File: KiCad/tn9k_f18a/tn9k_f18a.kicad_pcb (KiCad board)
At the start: 2 copper layers, 27.9 x 88.3 mm, 9 parts, among them J1 Conn_01x20, J2 Conn_01x20, J3 Conn_01x24, J4 Conn_01x24, J5 Conn_02x04_Counter_Clockwise, J6 Conn_02x08_Odd_Even, U1 SN74LVC245, U2 SN74LVC245, U3 SN74LVC245

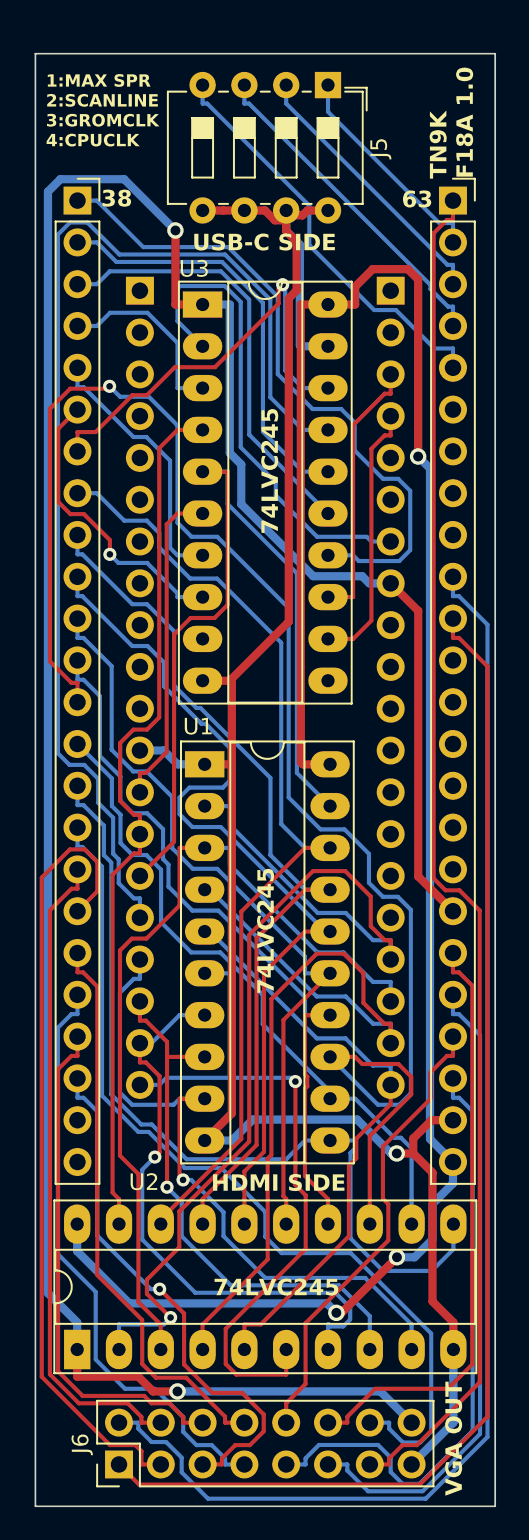
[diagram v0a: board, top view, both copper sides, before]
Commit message: update original board adding diode
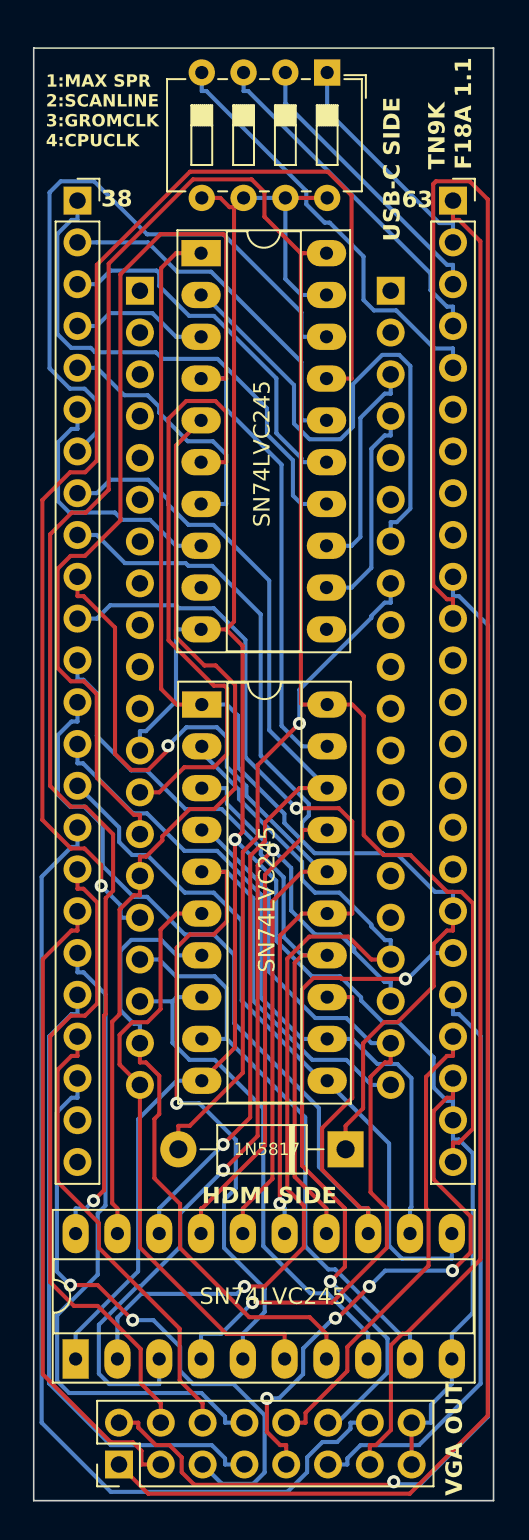
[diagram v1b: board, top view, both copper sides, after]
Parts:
- added D1: 1N5817, Diode_THT:D_DO-41_SOD81_P10.16mm_Horizontal, F.Cu at (166.2, 107.8)
- moved U2 39.9 mm to (157.4, 80.8), turned to 0 degrees
- moved U1 37.0 mm to (149.8, 120.6), turned to 90 degrees
- moved U3 3.12 mm to (157.4, 53.4)
- moved J5 0.76 mm to (165.0, 42.4)
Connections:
- J4 pad 18: VCC -> VDD
- J6 pad 16: VCC -> GND
- U2 pad 1: VCC -> VDD
- U3 pad 1: VCC -> VDD
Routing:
- net VCC: track 156.4 -> 40.4 mm, vias 2 -> 1
- net VDD: track 0.00 -> 72.4 mm
- net R0_3V3: track 74.2 -> 130.0 mm
- net CD5_3V3: track 98.6 -> 61.2 mm, vias 1 -> 0
- net ~{CSW}: track 53.5 -> 83.8 mm
- net GND: track 123.8 -> 151.6 mm
- net CD3: track 36.2 -> 57.9 mm, vias 0 -> 1
- net VCC_3V3: track 124.9 -> 145.9 mm, vias 3 -> 1
- net MODE: track 19.6 -> 37.3 mm
- net ~{RESET_3V3}: track 26.2 -> 39.9 mm, vias 1 -> 0
- net CD1: track 51.5 -> 61.5 mm, vias 0 -> 2
- net R2_3V3: track 48.1 -> 39.2 mm
- net CD7_3V3: track 52.0 -> 43.2 mm
- net MODE_3V3: track 40.3 -> 31.6 mm
- net CD3_3V3: track 46.9 -> 55.4 mm, vias 0 -> 2
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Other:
- board text added: "TN9K F18A 1.1"
- board text removed: "74LVC245"
- board text removed: "TN9K F18A 1.0"
